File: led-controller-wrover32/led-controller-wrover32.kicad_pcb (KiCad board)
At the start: 2 copper layers, 36 x 36 mm, 51 parts, among them J1 Micro_SD_Card, J2 Conn_01x12, J3 USB_B_Micro, J4 Conn_01x12, J5 Conn_01x04 DNS, J6 Conn_01x02 DNS, J7 Conn_01x03, J8 Conn_01x05, Q1 MMBT2222A-TP, Q2 MMBT2222A-TP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

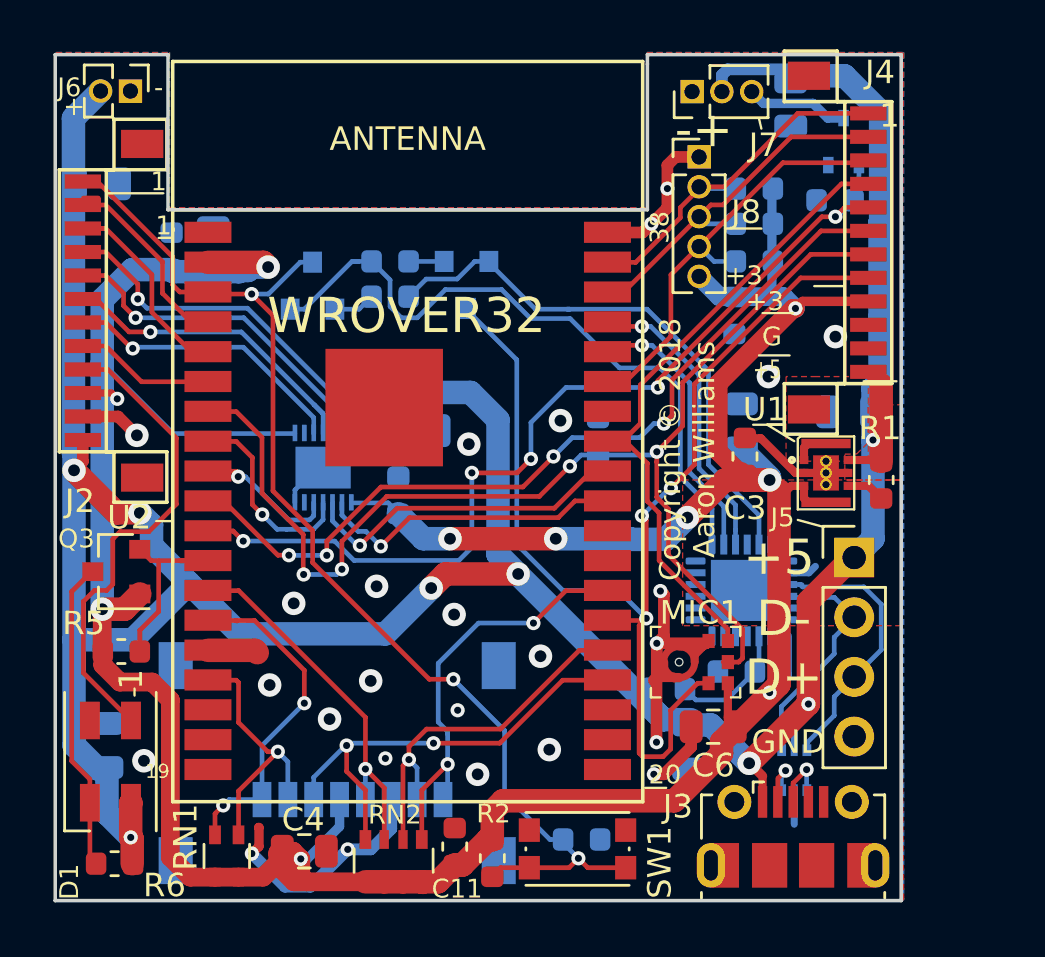
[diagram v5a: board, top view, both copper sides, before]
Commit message: Minor cleanup. - Removed overlapping fiducials (which aren't really needed) - Changed 3 pull-up resistors for IO21, IO22 and IO23 to use a   resistor network and moved further away from J8 - Fixed unconnected pull-up for IO15 (hopefully it was connected in 1.4) - Bumped to 1.4.2
Signed-off-by: Aaron Williams <aaron.w2@gmail.com>
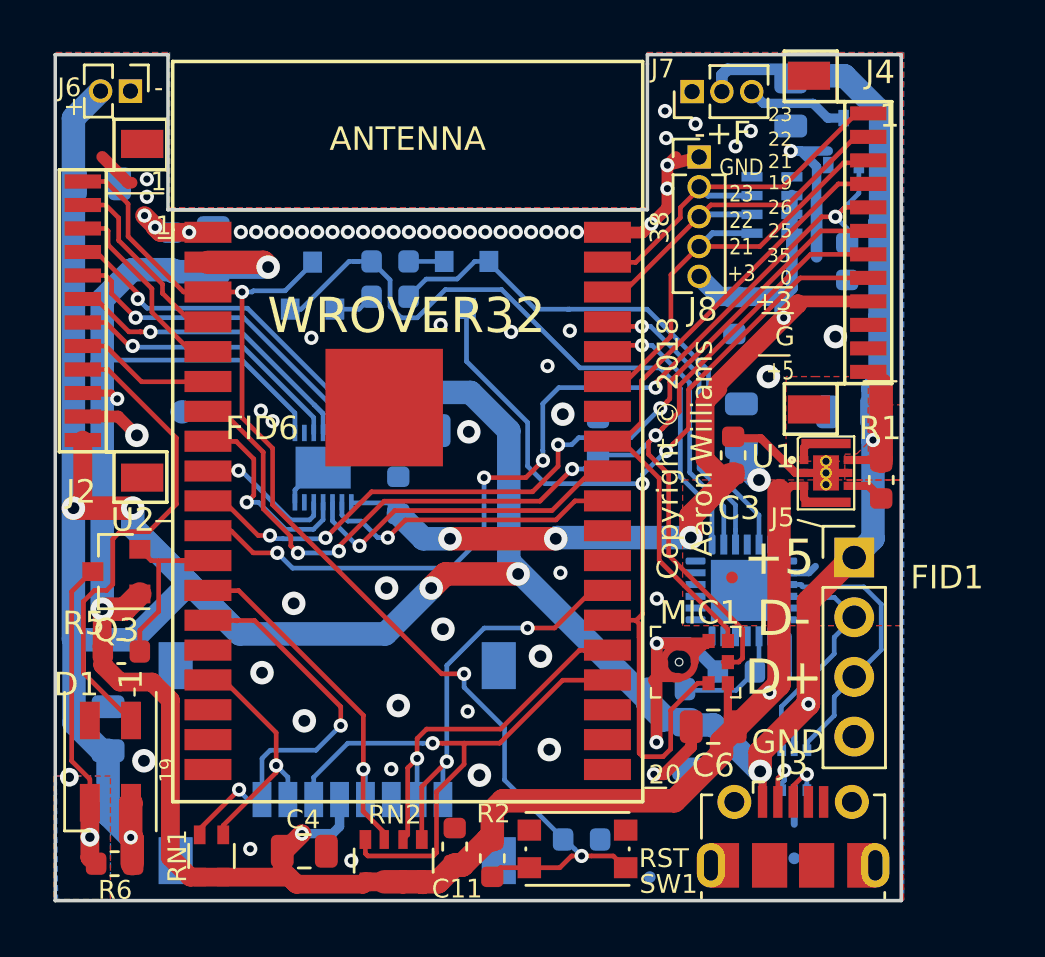
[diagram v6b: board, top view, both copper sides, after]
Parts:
- removed R7, R8, R9: 10K, Resistor_SMD:R_0603_1608Metric
- added FID1: FIDUCIAL_1MM, Fiducials:Fiducial_0.5mm_Dia_1mm_Outer, F.Cu at (78.8, 64.2)
- added FID2: FIDUCIAL_1MM, Fiducials:Fiducial_0.5mm_Dia_1mm_Outer, B.Cu at (81.5, 76.2)
- added FID3: FIDUCIAL_1MM, Fiducials:Fiducial_0.5mm_Dia_1mm_Outer, B.Cu at (75.3, 77.0)
- added FID6: FIDUCIAL_1MM, Fiducials:Fiducial_1mm_Dia_2.54mm_Outer_CopperBottom, F.Cu at (55.4, 57.2)
- added RN3: R_Pack04, Resistor_SMD:R_Array_Concave_4x0603, B.Cu at (80.5, 48.4)
- D1: footprint LED_SMD:LED_SK6812MINI_PLCC4_3.5x3.5mm_P1.75mm -> Aaron:LED_SK6812MINI_PLCC4_3.5x3.5mm_P1.75mm
- D2: footprint TO_SOT_Packages_SMD:SOT-666 -> Package_TO_SOT_SMD:SOT-666
- J3: footprint Connectors_USB:USB_Micro-B_Molex-105017-0001 -> Aaron:USB_Micro-B_Molex-105017-0001
- J7: value Conn_01x03 -> Conn_01x03 DNS
- Q1, Q2, Q3: footprint TO_SOT_Packages_SMD:SOT-23 -> Package_TO_SOT_SMD:SOT-23
- SW1: footprint Buttons_Switches_SMD:SW_SPST_KMR2 -> Aaron:SW_SPST_KMR2
- U3: footprint Housings_DFN_QFN:QFN-24-1EP_4x4mm_Pitch0.5mm_rounded_corners -> Aaron:QFN-24-1EP_4x4mm_Pitch0.5mm_rounded_corners
- moved R11 2.65 mm to (83.7, 50.8), turned to 270 degrees
- moved C9 0.71 mm to (52.2, 70.7)
- moved RN1 0.65 mm to (56.6, 76.1)
- moved C3 0.50 mm to (78.8, 59.0)
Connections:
- net /FET_1A renamed Net-(J7-Pad3)
- net Net-(D1-Pad3) renamed /IO27_5V
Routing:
- net +3V3: track 159.5 -> 145.9 mm
- net /IO0: track 50.8 -> 46.0 mm, vias 3 -> 2
- net /IO15: track 19.5 -> 24.2 mm, vias 2 -> 1
- net /IO12: track 14.4 -> 17.5 mm
- net /IO35: track 52.2 -> 50.7 mm
- net /IO26: track 40.8 -> 42.3 mm
- net /IO13: track 11.7 -> 10.8 mm
- net /IO25: track 35.9 -> 35.1 mm
- net /SENSOR_VN: track 9.29 -> 8.44 mm
- net /IO23: track 15.7 -> 16.4 mm
- net /SENSOR_VP: track 8.81 -> 8.17 mm
- net /IO21: track 18.4 -> 19.0 mm
- net /IO4: track 18.4 -> 17.8 mm
- net VBUS: track 144.6 -> 145.2 mm
- net /IO22: track 16.3 -> 16.8 mm
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- added copper zone on B.Cu, net /IO27_5V
- added copper zone on F.Cu, net /IO27_5V
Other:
- board text added: "-+F"
- board text added: "0"
- board text added: "21"
- board text added: "22"
- board text added: "23"
- board text added: "25"
- board text added: "26"
- board text added: "35"
- board text added: "GND 23 22 21 +3"
- board text added: "RST"
- board text added: "Rev 1.4.2"
- board text removed: "-+"
- board text removed: "Rev 1.4"

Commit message: Fixed solder mask clearance.
Signed-off-by: Aaron Williams <aaron.w2@gmail.com>
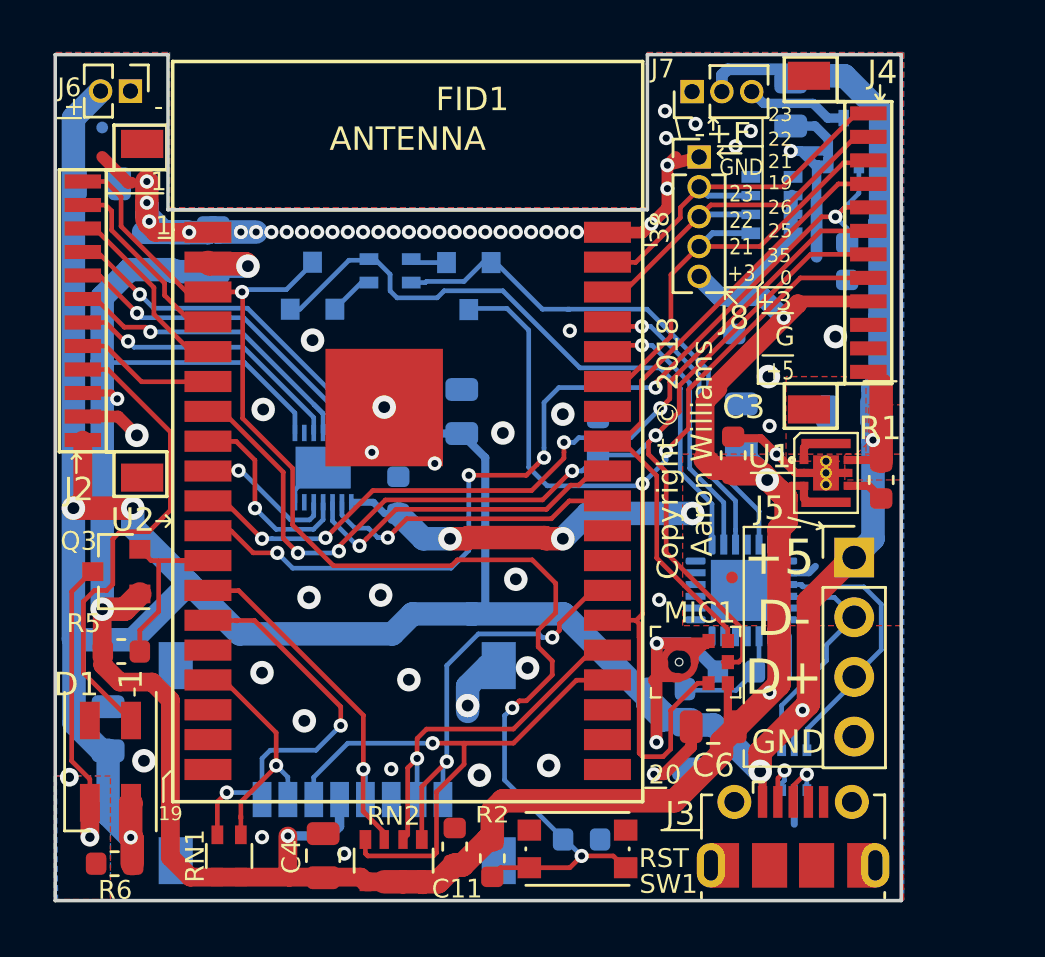
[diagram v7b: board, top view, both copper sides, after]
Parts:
- removed FID6: FIDUCIAL_1MM, Fiducials:Fiducial_1mm_Dia_2.54mm_Outer_CopperBottom
- removed R3, R4: 10K, Resistor_SMD:R_0603_1608Metric
- added RN4: R_Pack02, Resistor_SMD:R_Array_Convex_2x0603, B.Cu at (64.2, 51.2)
- RN3: footprint Resistor_SMD:R_Array_Concave_4x0603 -> Resistor_SMD:R_Array_Convex_4x0603
- moved FID3 39.5 mm to (52.0, 45.1)
- moved C7 2.07 mm to (67.3, 57.2), turned to 90 degrees
- moved FID2 1.10 mm to (82.2, 77.0)
- moved C4 0.82 mm to (61.4, 76.1), turned to 90 degrees
- moved RN1 0.75 mm to (57.4, 76.1)
- moved Q1 0.11 mm to (67.6, 51.9)
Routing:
- net GND: track 50.2 -> 66.2 mm, vias 68 -> 67
- net /RESET: track 50.5 -> 57.6 mm
- net VBUS: track 145.2 -> 141.5 mm, vias 8 -> 6
- net /IO27_5V: track 13.7 -> 12.0 mm
- net /RTS: track 28.9 -> 27.3 mm
- net /IO0: track 46.0 -> 47.1 mm
- net +3V3: track 145.9 -> 146.4 mm
- net /DTR: track 23.9 -> 23.4 mm
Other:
- rule pad_to_mask_clearance: 0.2 -> 0.0508
- rule trace_min: 0.17 -> 0.2
- board text added: "Micro SD"
- board text added: "Rev 1.4.3"
- board text removed: "Rev 1.4.2"
- board text removed: "WROVER32"
